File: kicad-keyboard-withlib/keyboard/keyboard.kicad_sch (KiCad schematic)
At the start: 47 parts, among them SW1 SW_Push, SW10 SW_Push, SW11 SW_Push, SW12 SW_Push, SW13 SW_Push, SW14 SW_Push, SW15 SW_Push, SW16 SW_Push, SW17 SW_Push, SW18 SW_Push, SW19 SW_Push, SW2 SW_Push, SW20 SW_Push, SW21 SW_Push, SW22 SW_Push, SW23 SW_Push, SW24 SW_Push, SW25 SW_Push, SW26 SW_Push, SW27 SW_Push, SW28 SW_Push, SW29 SW_Push, SW3 SW_Push, SW30 SW_Push, SW31 SW_Push, SW32 SW_Push, SW33 SW_Push, SW34 SW_Push, SW35 SW_Push, SW36 SW_Push, SW37 SW_Push, SW38 SW_Push, SW39 SW_Push, SW4 SW_Push, SW40 SW_Push, SW41 RotaryEncoder_Switch, SW42 SW_Wuerth_450301014042, SW5 SW_Push, SW6 SW_Push, SW7 SW_Push, SW8 SW_Push, SW9 SW_Push, U1 ATmega2560-16A, U2 MCP23017_SO

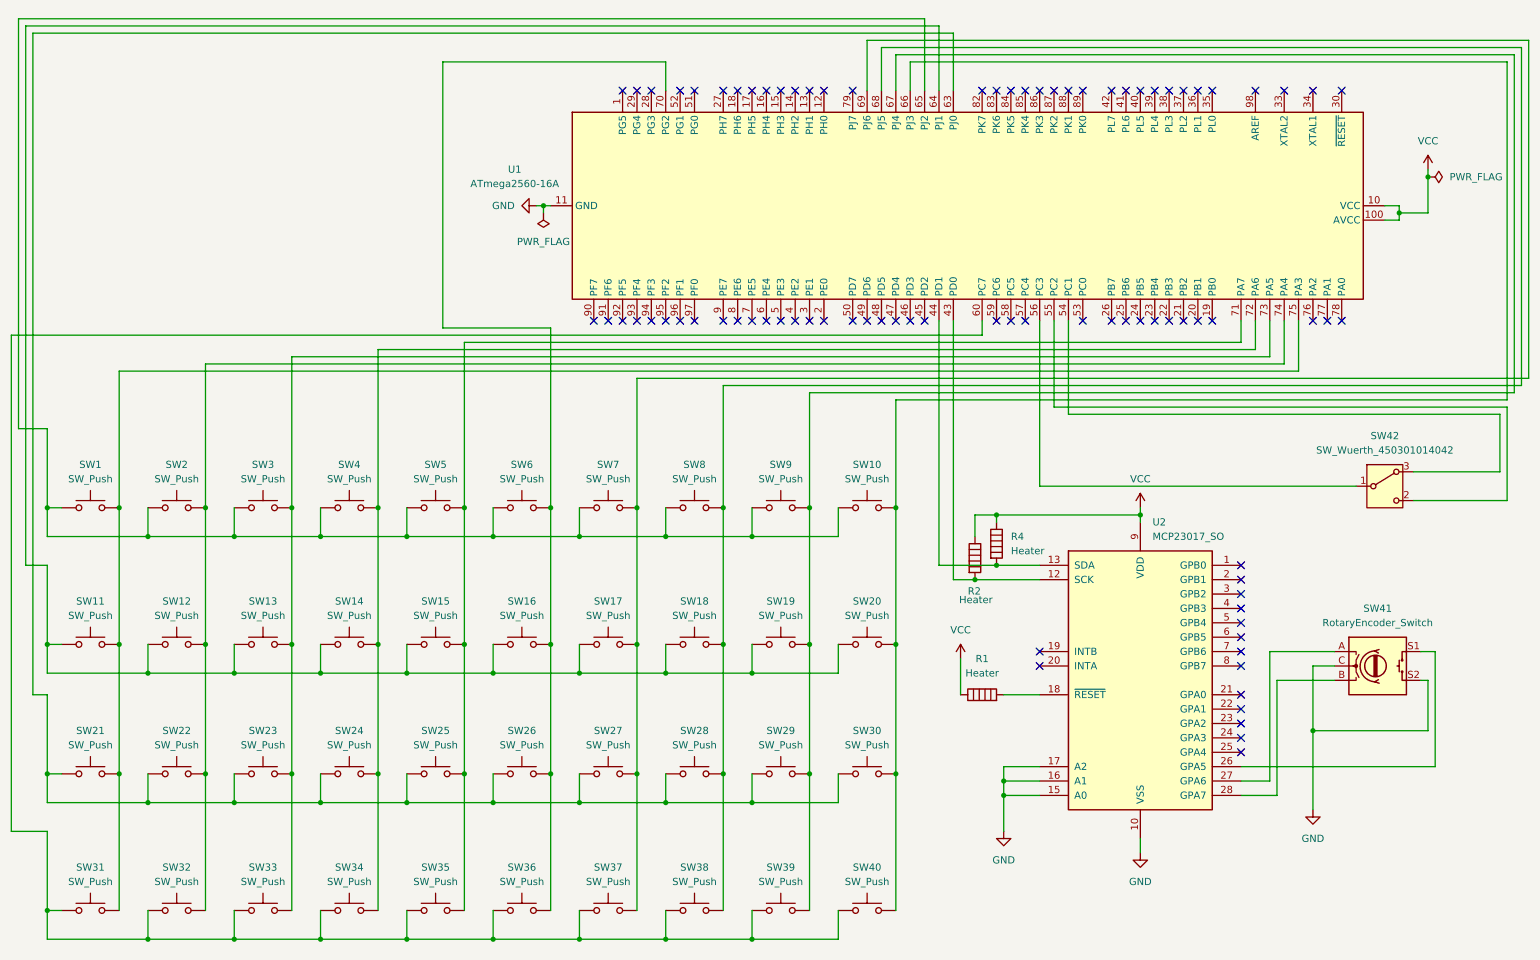
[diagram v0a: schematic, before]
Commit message: fix: - atmega + pinsocket in keyboard schematic
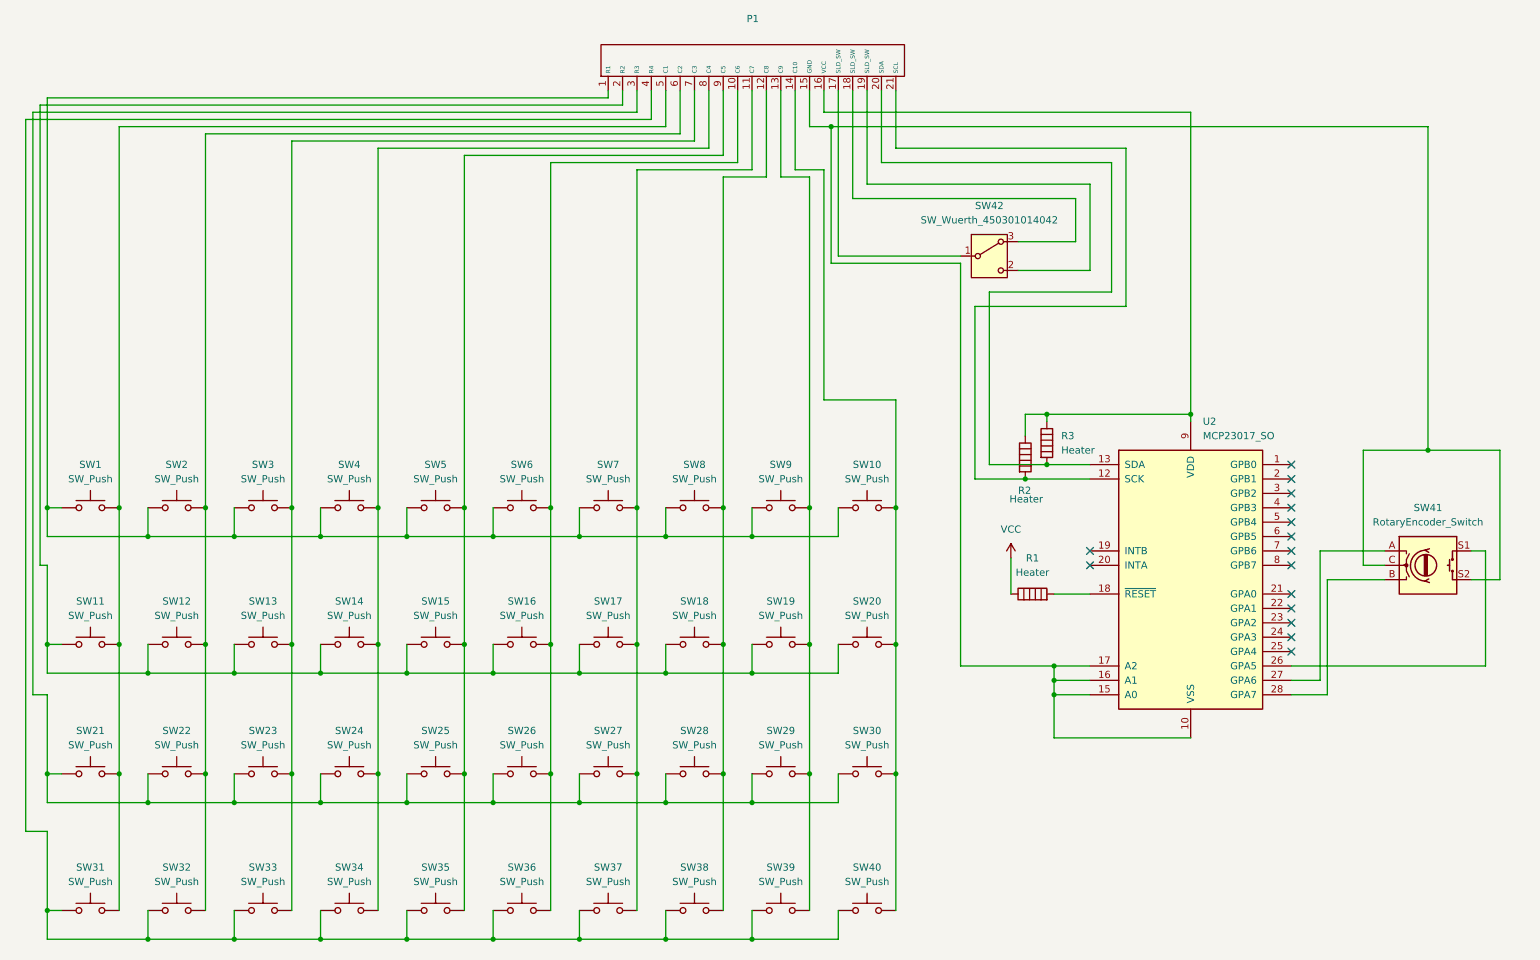
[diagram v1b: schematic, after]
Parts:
- removed U1: ATmega2560-16A, Package_QFP:TQFP-100_14x14mm_P0.5mm, symbol MCU_Microchip_ATmega:ATmega2560-16A
- added P1: ~, symbol Lilyspad:pin_socket
- renumbered R4 to R3
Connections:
- net VCC: no longer R2.1, R3.1, U2.9 (VDD)
- net at SW11.1, SW12.1, SW13.1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: now also P1.2 (R2)
- net at SW15.2, SW25.2, SW35.2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: now also P1.9 (C5)
- net at R2.2, U2.12 (SCK): now also P1.21 (SCL)
- net at R3.2, U2.13 (SDA): now also P1.20 (SDA)
- net at SW21.1, SW22.1, SW23.1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: now also P1.3 (R3)
- net at SW14.2, SW24.2, SW34.2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: now also P1.8 (C4)
- net at SW42.1 (B): now also P1.17 (SLD_SW)
- net at SW42.2 (C): now also P1.19 (SLD_SW)
- net at SW42.3 (A): now also P1.18 (SLD_SW)
- net at SW1.1, SW10.1, SW2.1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: now also P1.1 (R1)
- net at SW31.1, SW32.1, SW33.1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: now also P1.4 (R4)
- net at SW12.2, SW2.2, SW22.2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: now also P1.6 (C2)
- net at SW19.2, SW29.2, SW39.2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: now also P1.13 (C9)
- net at SW10.2, SW20.2, SW30.2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: now also P1.14 (C10)
- net at SW13.2, SW23.2, SW3.2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: now also P1.7 (C3)
- net at SW16.2, SW26.2, SW36.2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: now also P1.10 (C6)
- net at SW17.2, SW27.2, SW37.2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: now also P1.11 (C7)
- net at SW1.2, SW11.2, SW21.2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: now also P1.5 (C1)
- net at SW18.2, SW28.2, SW38.2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: now also P1.12 (C8)
- net GND: no longer names the net of SW41.C, SW41.S2, U2.10 (VSS), U2.15 (A0), U2.16 (A1), U2.17 (A2)
- net GND: now also P1.15 (GND)
- new net: P1.16 (VCC), R2.1, R3.1, U2.9 (VDD)
- no-connect marks 86 -> 15
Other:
- moved on the sheet: R1, R2, R3, SW41, SW42, U2

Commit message: add: linked footprint
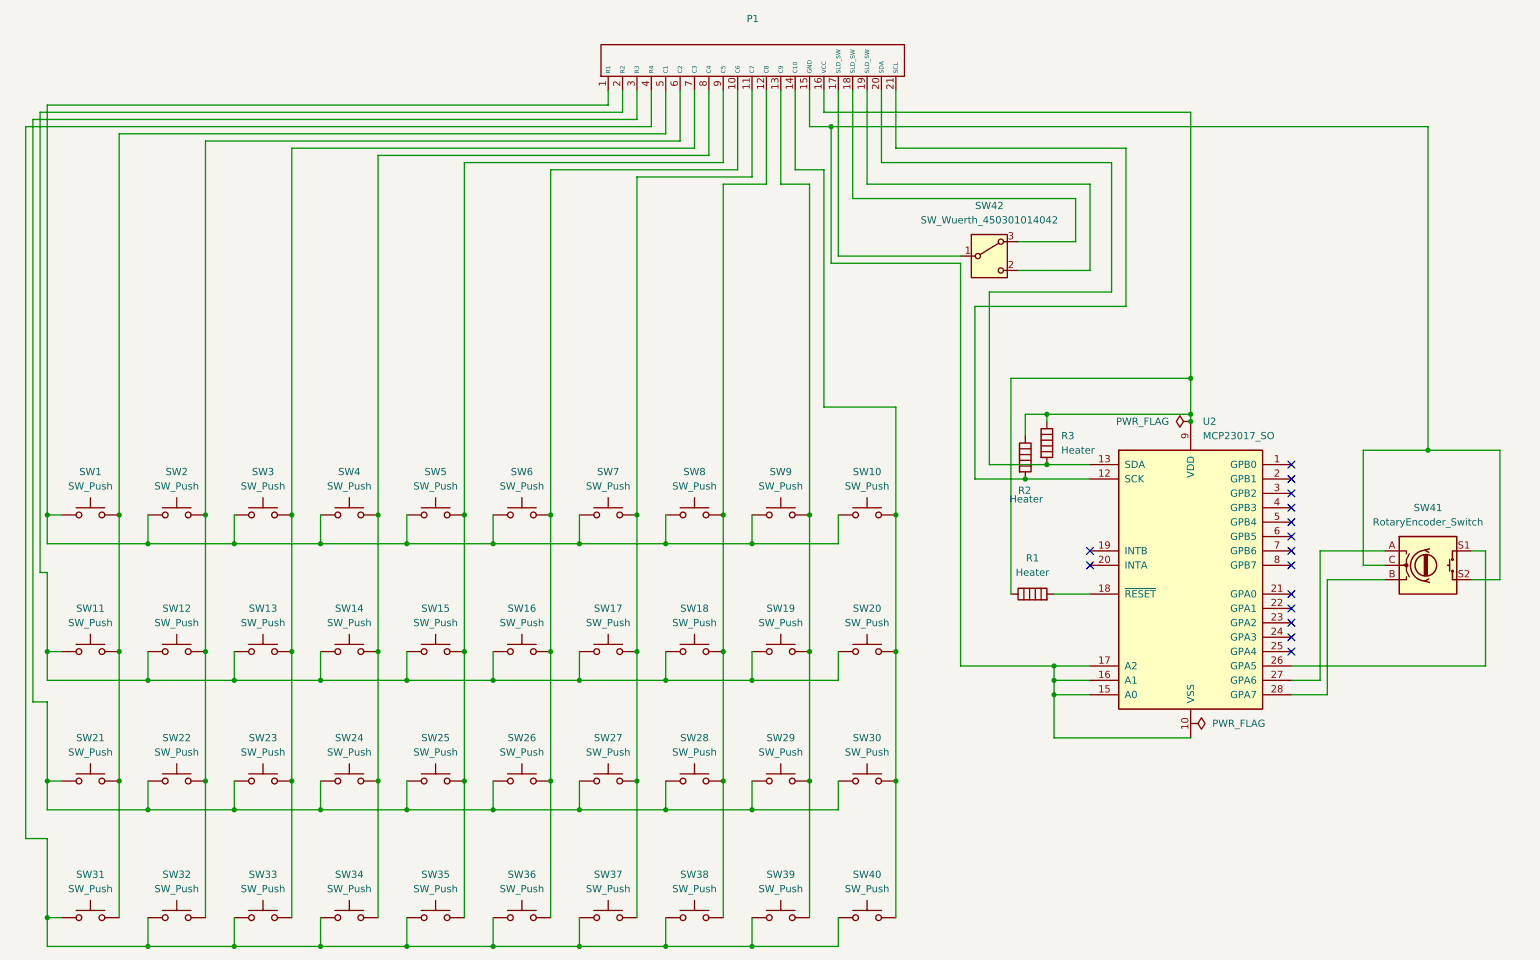
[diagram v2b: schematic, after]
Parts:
- R1, R3: footprint (none) -> Resistor_SMD:R_0201_0603Metric
- SW1, SW10, SW11, SW12, SW13, SW14, SW15, SW16, SW17, SW18, SW19, SW2, SW20, SW21, SW22, SW23, SW24, SW25, SW26, SW27, SW28, SW29, SW3, SW30, SW31, SW32, SW33, SW34, SW35, SW36, SW37, SW38, SW39, SW4, SW40, SW5, SW6, SW7, SW8, SW9: footprint (none) -> Button_Switch_THT:SW_PUSH-12mm_Wuerth-430476085716
- SW41: footprint (none) -> Rotary_Encoder:RotaryEncoder_Alps_EC11E-Switch_Vertical_H20mm
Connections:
- net VCC is gone; now on an unnamed net: R1.1
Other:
- moved on the sheet: SW1, SW10, SW11, SW12, SW13, SW14, SW15, SW16, SW17, SW18, SW19, SW2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
